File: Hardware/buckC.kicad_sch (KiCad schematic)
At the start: 32 parts, among them U6 SiC431

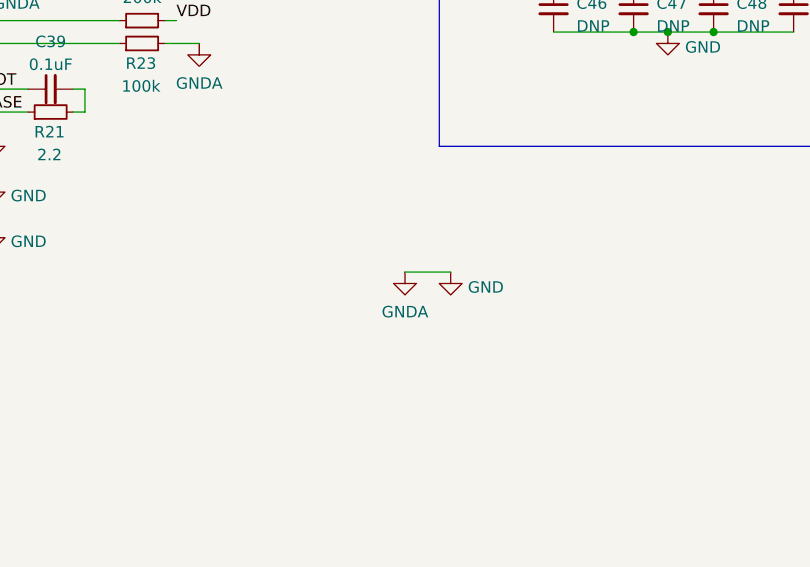
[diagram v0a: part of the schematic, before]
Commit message: pyro channels & tiny buck passives
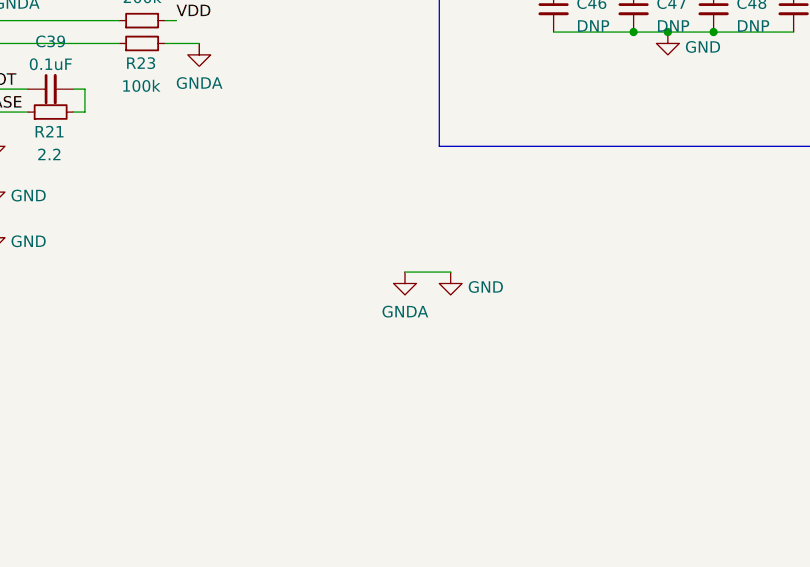
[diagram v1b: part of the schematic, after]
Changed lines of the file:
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@@
+    (stroke (width 0) (type default))
+  )
+  (wire (pts (xy 186.69 115.57) (xy 191.77 115.57))
     (stroke (width 0) (type default))
   )
@@
   )
   (wire (pts (xy 81.28 85.09) (xy 93.98 85.09))
-    (stroke (width 0) (type default))
-  )
-  (wire (pts (xy 186.69 115.57) (xy 191.77 115.57))
     (stroke (width 0) (type default))
   )
@@
     )
   )
-  (symbol (lib_id "power:GNDA") (at 186.69 115.57 0) (mirror y) (unit 1)
+  (symbol (lib_id "power:GNDA") (at 186.69 115.57 0) (unit 1)
     (in_bom yes) (on_board yes) (dnp no)
     (property "Reference" "#PWR072" (at 186.69 121.92 0)

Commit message: High power side nearly done
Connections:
- net MODE2: now reaches R22.1, U6.20 (MODE_2)
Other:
- note added: "499k = 32A 200k = 25A 100k = 17A 51k = 9.6A"
- note added: "Current limit set resistor"
- moved on the sheet: C41, C42, C43, C44, C45, C46, C47, C48, C49

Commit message: high V side finished, CAN circuit and ESP left to place
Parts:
- removed C40: 47uF, Capacitor_SMD:C_1206_3216Metric, symbol Device:C_Small
- removed C45: DNP, Capacitor_SMD:C_1206_3216Metric, symbol Device:C_Small
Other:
- moved on the sheet: C38

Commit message: finished? (pre-review)
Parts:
- removed C46, C48, C49: DNP, Capacitor_SMD:C_1206_3216Metric, symbol Device:C_Small
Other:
- moved on the sheet: C47
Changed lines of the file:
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@@
 (kicad_sch (version 20230121) (generator eeschema)
   (paper "A4")
-  (junction (at 232.41 53.34) (diameter 0) (color 0 0 0 0)
-  )
   (junction (at 220.98 34.29) (diameter 0) (color 0 0 0 0)
   )
@@
   (junction (at 229.87 39.37) (diameter 0) (color 0 0 0 0)
   )
-  (junction (at 214.63 58.42) (diameter 0) (color 0 0 0 0)
-  )
   (junction (at 64.77 34.29) (diameter 0) (color 0 0 0 0)
   )
@@
   (junction (at 59.69 39.37) (diameter 0) (color 0 0 0 0)
   )
-  (junction (at 214.63 53.34) (diameter 0) (color 0 0 0 0)
-  )
   (junction (at 217.17 34.29) (diameter 0) (color 0 0 0 0)
   )
@@
   (junction (at 101.6 142.24) (diameter 0) (color 0 0 0 0)
   )
-  (junction (at 218.44 58.42) (diameter 0) (color 0 0 0 0)
-  )
   (junction (at 106.68 142.24) (diameter 0) (color 0 0 0 0)
   )
@@
   )
   (junction (at 68.58 39.37) (diameter 0) (color 0 0 0 0)
-  )
-  (junction (at 223.52 58.42) (diameter 0) (color 0 0 0 0)
-  )
-  (junction (at 223.52 53.34) (diameter 0) (color 0 0 0 0)
   )
   (junction (at 143.51 76.2) (diameter 0) (color 0 0 0 0)
@@
     (stroke (width 0) (type default))
   )
-  (wire (pts (xy 205.74 53.34) (xy 214.63 53.34))
-    (stroke (width 0) (type default))
-  )
   (wire (pts (xy 209.55 99.06) (xy 218.44 99.06))
     (stroke (width 0) (type default))
@@
     (stroke (width 0) (type default))
   )
-  (wire (pts (xy 214.63 58.42) (xy 218.44 58.42))
-    (stroke (width 0) (type default))
-  )
   (wire (pts (xy 129.54 80.01) (xy 139.7 80.01))
     (stroke (width 0) (type default))
@@
     (stroke (width 0) (type default))
   )
-  (wire (pts (xy 218.44 58.42) (xy 223.52 58.42))
-    (stroke (width 0) (type default))
-  )
   (polyline (pts (xy 96.52 26.67) (xy 96.52 46.99))
     (stroke (width 0) (type default))
@@
     (stroke (width 0) (type default))
   )
-  (wire (pts (xy 219.71 53.34) (xy 223.52 53.34))
+  (wire (pts (xy 219.71 53.34) (xy 241.3 53.34))
     (stroke (width 0) (type default))
   )
@@
     (stroke (width 0) (type default))
   )
-  (wire (pts (xy 205.74 58.42) (xy 214.63 58.42))
-    (stroke (width 0) (type default))
-  )
   (wire (pts (xy 110.49 142.24) (xy 119.38 142.24))
     (stroke (width 0) (type default))
   )
-  (wire (pts (xy 223.52 58.42) (xy 232.41 58.42))
-    (stroke (width 0) (type default))
-  )
   (wire (pts (xy 64.77 34.29) (xy 68.58 34.29))
     (stroke (width 0) (type default))
@@
     (stroke (width 0) (type default))
   )
-  (wire (pts (xy 232.41 53.34) (xy 241.3 53.34))
-    (stroke (width 0) (type default))
-  )
   (wire (pts (xy 106.68 142.24) (xy 110.49 142.24))
     (stroke (width 0) (type default))
@@
     (stroke (width 0) (type default))
   )
-  (wire (pts (xy 223.52 53.34) (xy 232.41 53.34))
-    (stroke (width 0) (type default))
-  )
   (wire (pts (xy 93.98 77.47) (xy 93.98 78.74))
     (stroke (width 0) (type default))
@@
     (stroke (width 0) (type default))
   )
-  (wire (pts (xy 214.63 53.34) (xy 219.71 53.34))
+  (wire (pts (xy 218.44 53.34) (xy 219.71 53.34))
     (stroke (width 0) (type default))
   )
@@
     )
   )
-  (symbol (lib_id "Device:C_Small") (at 205.74 55.88 0) (unit 1)
-    (in_bom yes) (on_board yes) (dnp no) (fields_autoplaced)
-    (property "Reference" "C46" (at 208.28 55.2513 0)
-      (effects (font (size 1.27 1.27)) (justify left))
-    )
-    (property "Value" "DNP" (at 208.28 57.7913 0)
-      (effects (font (size 1.27 1.27)) (justify left))
-    )
-    (property "Footprint" "Capacitor_SMD:C_1206_3216Metric" (at 205.74 55.88 0)
-      (effects (font (size 1.27 1.27)) hide)
-    )
-    (property "Datasheet" "~" (at 205.74 55.88 0)
-      (effects (font (size 1.27 1.27)) hide)
-    )
-    (pin "1")
-    (pin "2")
-    (instances
-      (project "buckC"
-        (path "/292a7663-8ba4-4680-a4b9-031ee4118f85"
-          (reference "C46") (unit 1)
-        )
-      )
-      (project "flintandsteel"
-        (path "/7db990e4-92e1-4f99-b4d2-435bbec1ba83/789c80db-ca1a-4c36-a832-c7a232b1153f"
-          (reference "C43") (unit 1)
-        )
-      )
-    )
-  )
   (symbol (lib_id "power:GND") (at 140.97 105.41 0) (unit 1)
     (in_bom yes) (on_board yes) (dnp no) (fields_autoplaced)
@@
     )
   )
-  (symbol (lib_id "Device:C_Small") (at 214.63 55.88 0) (unit 1)
+  (symbol (lib_id "Device:C_Small") (at 218.44 55.88 0) (unit 1)
     (in_bom yes) (on_board yes) (dnp no) (fields_autoplaced)
-    (property "Reference" "C47" (at 217.17 55.2513 0)
-      (effects (font (size 1.27 1.27)) (justify left))
-    )
-    (property "Value" "DNP" (at 217.17 57.7913 0)
-      (effects (font (size 1.27 1.27)) (justify left))
-    )
-    (property "Footprint" "Capacitor_SMD:C_1206_3216Metric" (at 214.63 55.88 0)
-      (effects (font (size 1.27 1.27)) hide)
-    )
-    (property "Datasheet" "~" (at 214.63 55.88 0)
+    (property "Reference" "C47" (at 220.98 55.2513 0)
+      (effects (font (size 1.27 1.27)) (justify left))
+    )
+    (property "Value" "DNP" (at 220.98 57.7913 0)
+      (effects (font (size 1.27 1.27)) (justify left))
+    )
+    (property "Footprint" "Capacitor_SMD:C_1206_3216Metric" (at 218.44 55.88 0)
+      (effects (font (size 1.27 1.27)) hide)
+    )
+    (property "Datasheet" "~" (at 218.44 55.88 0)
       (effects (font (size 1.27 1.27)) hide)
     )
@@
         (path "/7db990e4-92e1-4f99-b4d2-435bbec1ba83/789c80db-ca1a-4c36-a832-c7a232b1153f"
           (reference "#PWR072") (unit 1)
-        )
-      )
-    )
-  )
-  (symbol (lib_id "Device:C_Small") (at 232.41 55.88 0) (unit 1)
-    (in_bom yes) (on_board yes) (dnp no) (fields_autoplaced)
-    (property "Reference" "C49" (at 234.95 55.2513 0)
-      (effects (font (size 1.27 1.27)) (justify left))
-    )
-    (property "Value" "DNP" (at 234.95 57.7913 0)
-      (effects (font (size 1.27 1.27)) (justify left))
-    )
-    (property "Footprint" "Capacitor_SMD:C_1206_3216Metric" (at 232.41 55.88 0)
-      (effects (font (size 1.27 1.27)) hide)
-    )
-    (property "Datasheet" "~" (at 232.41 55.88 0)
-      (effects (font (size 1.27 1.27)) hide)
-    )
-    (pin "1")
-    (pin "2")
-    (instances
-      (project "buckC"
-        (path "/292a7663-8ba4-4680-a4b9-031ee4118f85"
-          (reference "C49") (unit 1)
-        )
-      )
-      (project "flintandsteel"
-        (path "/7db990e4-92e1-4f99-b4d2-435bbec1ba83/789c80db-ca1a-4c36-a832-c7a232b1153f"
-          (reference "C49") (unit 1)
         )
       )
@@
         )
       )
-    )
-  )
-  (symbol (lib_id "Device:C_Small") (at 223.52 55.88 0) (unit 1)
-    (in_bom yes) (on_board yes) (dnp no) (fields_autoplaced)
-    (property "Reference" "C48" (at 226.06 55.2513 0)
-      (effects (font (size 1.27 1.27)) (justify left))
-    )
-    (property "Value" "DNP" (at 226.06 57.7913 0)
-      (effects (font (size 1.27 1.27)) (justify left))
-    )
-    (property "Footprint" "Capacitor_SMD:C_1206_3216Metric" (at 223.52 55.88 0)
-      (effects (font (size 1.27 1.27)) hide)
-    )
-    (property "Datasheet" "~" (at 223.52 55.88 0)
-      (effects (font (size 1.27 1.27)) hide)
-    )
-    (pin "1")
-    (pin "2")
-    (instances
-      (project "buckC"
-        (path "/292a7663-8ba4-4680-a4b9-031ee4118f85"
-          (reference "C48") (unit 1)
-        )
-      )
-      (project "flintandsteel"
-        (path "/7db990e4-92e1-4f99-b4d2-435bbec1ba83/789c80db-ca1a-4c36-a832-c7a232b1153f"
-          (reference "C47") (unit 1)
-        )
-      )

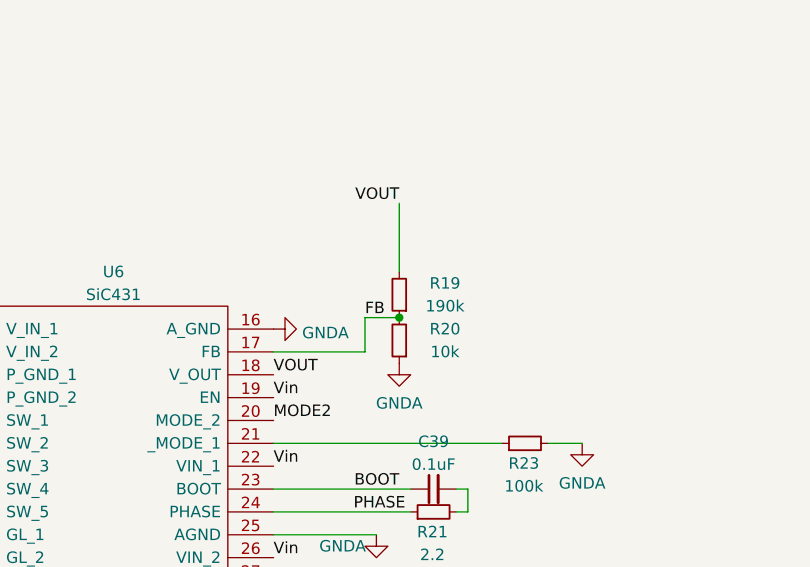
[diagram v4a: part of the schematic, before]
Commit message: changed buck FB resistors to actual values
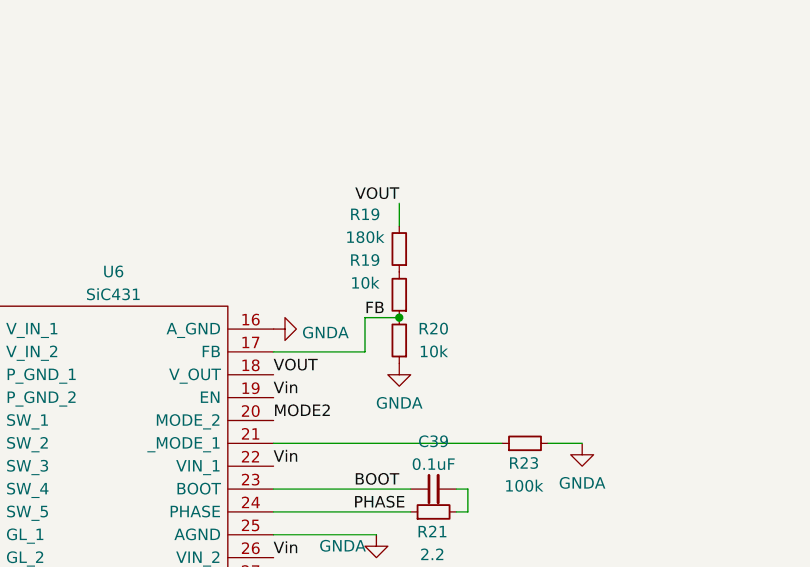
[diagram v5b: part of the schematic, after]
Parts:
- added R19: 180k, Capacitor_SMD:C_0402_1005Metric, symbol Device:R_Small
- R19: value 190k -> 10k
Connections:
- net +12V: now also R19.2; no longer R19.2
- new net: R19.1, R19.2
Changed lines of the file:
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@@
     (stroke (width 0) (type default))
   )
-  (wire (pts (xy 143.51 63.5) (xy 143.51 71.12))
+  (wire (pts (xy 143.51 63.5) (xy 143.51 66.04))
     (stroke (width 0) (type default))
   )
@@
   (symbol (lib_id "Device:R_Small") (at 143.51 73.66 180) (unit 1)
     (in_bom yes) (on_board yes) (dnp no)
-    (property "Reference" "R19" (at 148.59 72.39 0)
-      (effects (font (size 1.27 1.27)))
-    )
-    (property "Value" "190k" (at 148.59 74.9269 0)
+    (property "Reference" "R19" (at 139.7 69.85 0)
+      (effects (font (size 1.27 1.27)))
+    )
+    (property "Value" "10k" (at 139.7 72.3869 0)
       (effects (font (size 1.27 1.27)))
     )
@@
   (symbol (lib_id "Device:R_Small") (at 143.51 78.74 180) (unit 1)
     (in_bom yes) (on_board yes) (dnp no)
-    (property "Reference" "R20" (at 148.59 77.4731 0)
-      (effects (font (size 1.27 1.27)))
-    )
-    (property "Value" "10k" (at 148.59 80.01 0)
+    (property "Reference" "R20" (at 147.32 77.47 0)
+      (effects (font (size 1.27 1.27)))
+    )
+    (property "Value" "10k" (at 147.32 80.0069 0)
       (effects (font (size 1.27 1.27)))
     )
@@
         )
       )
+    )
+  )
+  (symbol (lib_id "Device:R_Small") (at 143.51 68.58 180) (unit 1)
+    (in_bom yes) (on_board yes) (dnp no)
+    (property "Reference" "R19" (at 139.7 64.77 0)
+      (effects (font (size 1.27 1.27)))
+    )
+    (property "Value" "180k" (at 139.7 67.3069 0)
+      (effects (font (size 1.27 1.27)))
+    )
+    (property "Footprint" "Capacitor_SMD:C_0402_1005Metric" (at 143.51 68.58 0)
+      (effects (font (size 1.27 1.27)) hide)
+    )
+    (property "Datasheet" "~" (at 143.51 68.58 0)
+      (effects (font (size 1.27 1.27)) hide)
+    )
+    (pin "1")
+    (pin "2")
+    (instances
+      (project "buckC"
+        (path "/292a7663-8ba4-4680-a4b9-031ee4118f85"
+          (reference "R19") (unit 1)
+        )
+      )
+      (project "flintandsteel"
+        (path "/7db990e4-92e1-4f99-b4d2-435bbec1ba83/789c80db-ca1a-4c36-a832-c7a232b1153f"
+          (reference "R39") (unit 1)
+        )
+      )
